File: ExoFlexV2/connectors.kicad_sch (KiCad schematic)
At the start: 48 parts, among them J10 EXT, J11 EVE, J12 DOR, J13 EXT, J14 EVE_AMP_LIM, J15 DOR_AMP_LIM, J16 EXT_AMP_LIM, J17 EVE_TOR_LIM, J18 DOR_TOR_LIM, J19 EXT_TOR_LIM, J8 EVE, J9 DOR

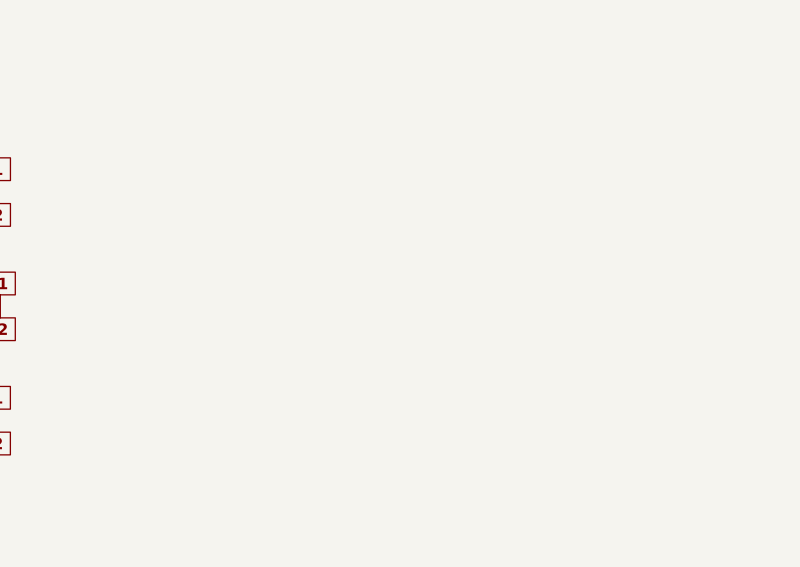
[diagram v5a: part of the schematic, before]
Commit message: Finalisation 1
- Ajout de pages pour la gestion des signaux négatif
- Modification des pages de torque et amplitude
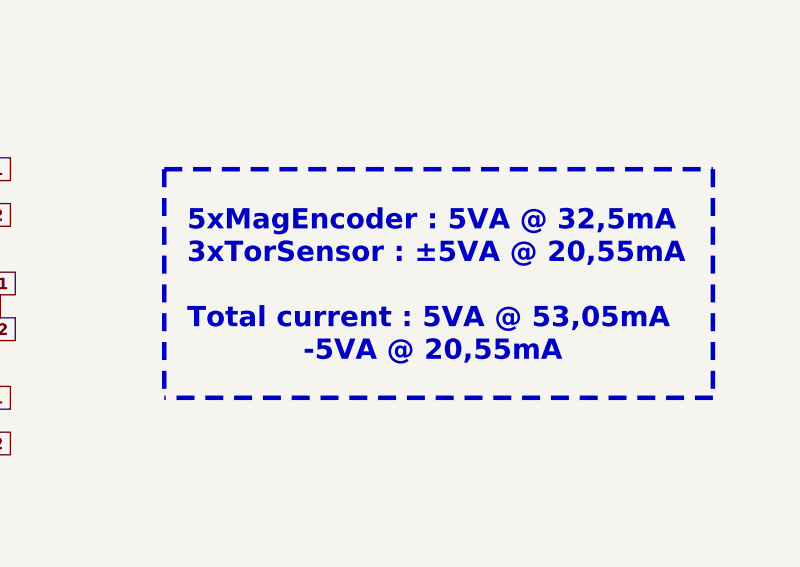
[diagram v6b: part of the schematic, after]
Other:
- note added: "5xMagEncoder : 5VA @ 32,5mA 3xTorSensor : ±5VA @ 20,55mA Total current : 5VA @ 53,05mA -5VA @ 20,55mA"
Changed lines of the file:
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@@
     (stroke (width 0) (type default) (color 0 0 0 0))
+  )
+  (polyline (pts (xy 222.25 33.02) (xy 222.25 58.42))
+    (stroke (width 0.5) (type dash) (color 255 148 44 1))
   )
   (wire (pts (xy 120.65 152.4) (xy 139.7 152.4))
@@
     (stroke (width 0) (type default) (color 0 0 0 0))
   )
+  (polyline (pts (xy 283.21 33.02) (xy 283.21 58.42))
+    (stroke (width 0.5) (type dash) (color 255 148 44 1))
+  )
   (wire (pts (xy 48.26 137.16) (xy 25.4 137.16))
     (stroke (width 0) (type default) (color 0 0 0 0))
@@
     (stroke (width 0) (type default) (color 0 0 0 0))
   )
+  (polyline (pts (xy 283.21 58.42) (xy 222.25 58.42))
+    (stroke (width 0.5) (type dash) (color 255 148 44 1))
+  )
   (wire (pts (xy 194.31 142.24) (xy 247.65 142.24))
     (stroke (width 0) (type default) (color 0 0 0 0))
@@
     (stroke (width 0) (type default) (color 0 0 0 0))
   )
+  (polyline (pts (xy 222.25 33.02) (xy 283.21 33.02))
+    (stroke (width 0.5) (type dash) (color 255 148 44 1))
+  )
   (wire (pts (xy 125.73 149.86) (xy 139.7 149.86))
     (stroke (width 0) (type default) (color 0 0 0 0))
@@
     (stroke (width 0) (type default) (color 0 0 0 0))
   )
+  (text "5xMagEncoder : 5VA @ 32,5mA\n3xTorSensor : ±5VA @ 20,55mA\n\nTotal current : 5VA @ 53,05mA\n		    -5VA @ 20,55mA"
+    (at 224.79 54.61 0)
+    (effects (font (size 2.25 2.25) (thickness 0.5) bold) (justify left bottom))
+  )
   (text "TORQUE" (at 13.97 91.44 0)
